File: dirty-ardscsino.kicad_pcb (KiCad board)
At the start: 2 copper layers, 42.7 x 75.2 mm, 16 parts, among them J1 SCSI, J2 171825-4 (Ext. Power), J3 DM3AT-SF-PEJM5, U1 STM32 Bluepill

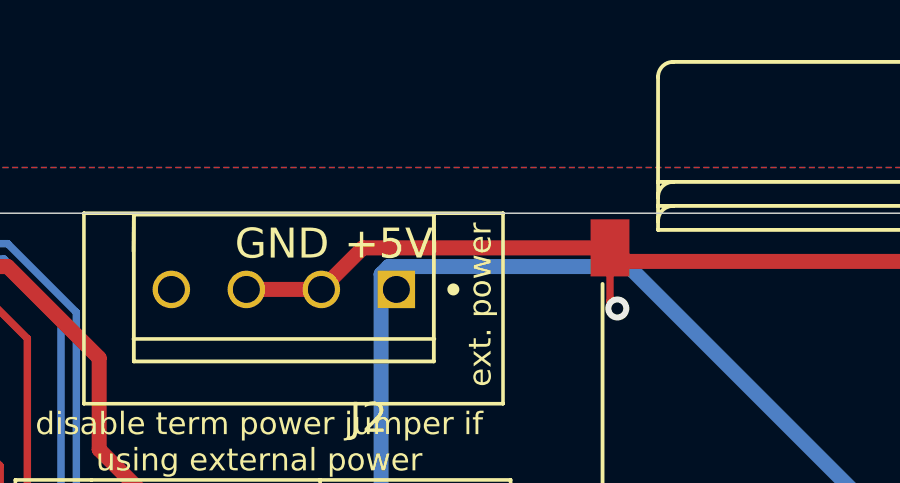
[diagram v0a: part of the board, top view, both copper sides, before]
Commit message: Flip power labels so you can read them
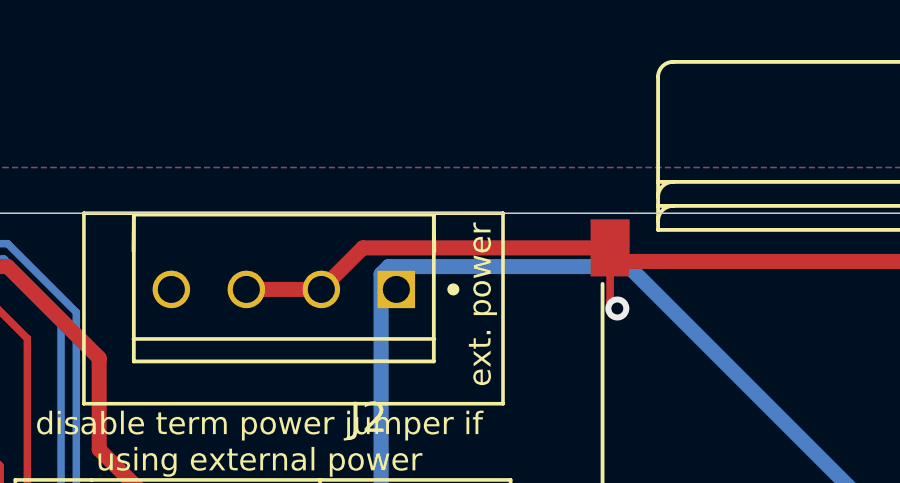
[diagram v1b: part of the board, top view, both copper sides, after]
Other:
- net class Default removed

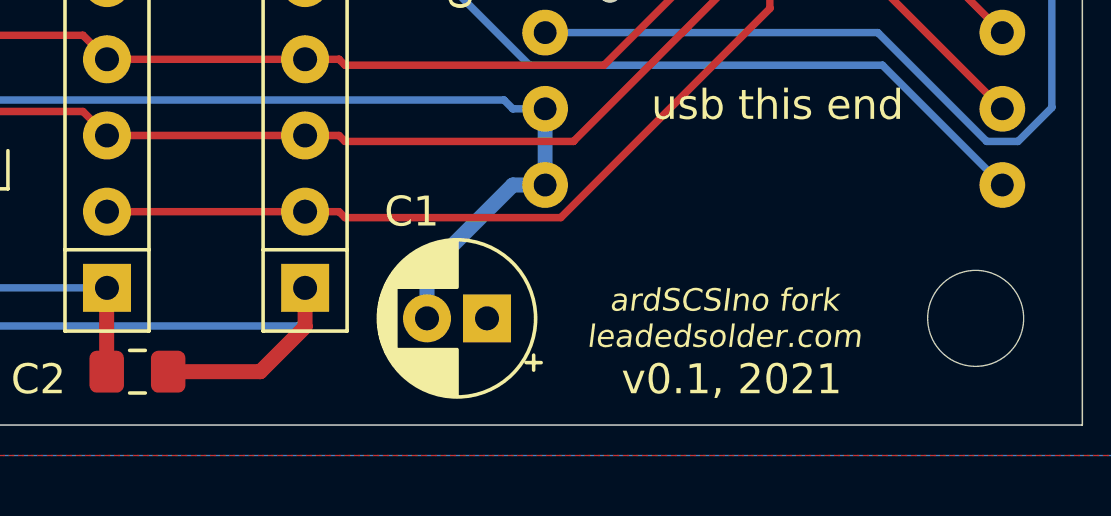
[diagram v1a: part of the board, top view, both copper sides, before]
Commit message: Improve assembly labeling
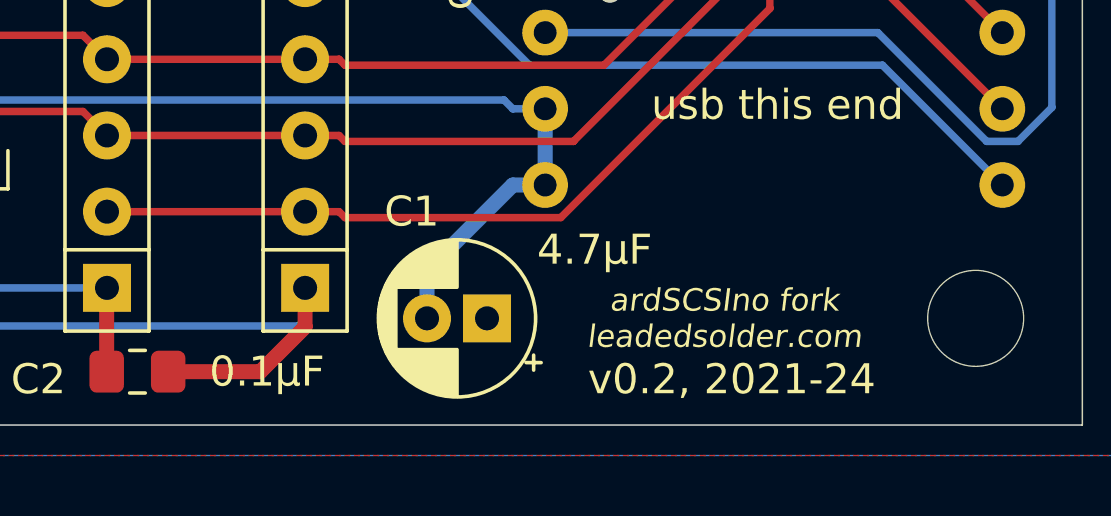
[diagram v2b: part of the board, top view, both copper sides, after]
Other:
- board text added: "v0.2, 2021-24"
- board text removed: "v0.1, 2021"
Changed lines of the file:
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@@
         (effects (font (size 1 1) (thickness 0.15)))
     )
-    (fp_text value "4.7µF" (at -0.762 3.81) (layer "F.Fab")
+    (fp_text value "4.7µF" (at -3.588 2.286) (layer "F.SilkS")
         (effects (font (size 1 1) (thickness 0.15)))
     )
@@
         (effects (font (size 1 1) (thickness 0.15)))
     )
-    (fp_text value "0.1µF" (at 0 1.65) (layer "F.Fab")
+    (fp_text value "0.1µF" (at 4.318 0) (layer "F.SilkS")
         (effects (font (size 1 1) (thickness 0.15)))
     )
@@
     (effects (font (size 0.75 0.75) (thickness 0.15)))
   )
-  (gr_text "v0.1, 2021" (at 165.1 149.86) (layer "F.SilkS")
+  (gr_text "v0.2, 2021-24" (at 165.1 149.86) (layer "F.SilkS")
     (effects (font (size 1 1) (thickness 0.15)))
   )

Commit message: Dirty ArdSCSIno 2 v1 sent to fab
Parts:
- removed JP2, JP3: Jumper_NC_Small, Connector_PinHeader_2.54mm:PinHeader_1x02_P2.54mm_Vertical
- removed REF** (x2): MountingHole_3.2mm_M3, MountingHole:MountingHole_3.2mm_M3
- removed REF**: OSHW-Logo2_14.6x12mm_SilkScreen, Symbol:OSHW-Logo2_14.6x12mm_SilkScreen
- added JP4: Jumper_2_Small_Bridged, Jumper:SolderJumper-2_P1.3mm_Bridged_RoundedPad1.0x1.5mm, F.Cu at (143.3, 118.5)
- added JP5: Jumper_2_Small_Bridged, Jumper:SolderJumper-2_P1.3mm_Bridged_RoundedPad1.0x1.5mm, F.Cu at (143.3, 122.0)
- added U2: microSD-Breakout, microSD_Breakout:microSD_AliExpress, F.Cu at (152.7, 93.8)
- C2: footprint Capacitor_SMD:C_0805_2012Metric_Pad1.15x1.40mm_HandSolder -> Capacitor_SMD:C_0805_2012Metric_Pad1.18x1.45mm_HandSolder
- JP1: value Jumper_NC_Small -> TERM_PWR_EN
- moved C2 100.5 mm to (122.5, 51.8), turned to 180 degrees
- moved J2 64.9 mm to (112.0, 127.0), turned to 90 degrees
- moved RN1 52.2 mm to (120.0, 55.0)
- moved RN2 46.3 mm to (125.0, 55.0)
- moved J1 43.8 mm to (106.7, 113.5)
- moved U1 43.5 mm to (139.0, 87.3)
- moved C1 43.4 mm to (119.2, 126.2), turned to 90 degrees
- moved RN4 41.9 mm to (120.0, 118.5)
- moved JP1 39.4 mm to (134.2, 124.7), turned to 0 degrees
- moved RN3 34.2 mm to (125.0, 118.5)
- moved J3 32.7 mm to (152.7, 120.4), turned to 90 degrees
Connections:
- C2 pad 1: Net-(C2-Pad1) -> GND
- C2 pad 2: Net-(C2-Pad2) -> +5V
- J1 pad 25: Net-(J1-Pad25) -> unconnected-(J1-Pin_25-Pad25)
- J2 pad 4: Net-(J2-Pad4) -> unconnected-(J2-Pad4)
- J3 pad 1: Net-(J3-Pad1) -> unconnected-(J3-DAT2-Pad1)
- J3 pad 8: Net-(J3-Pad8) -> unconnected-(J3-DAT1-Pad8)
- J3 pad SWA: Net-(J3-PadSWA) -> unconnected-(J3-PadSWA)
- J3 pad SWB: Net-(J3-PadSWB) -> unconnected-(J3-PadSWB)
- RN1 pad 1: Net-(C2-Pad2) -> +5V
- RN2 pad 1: Net-(C2-Pad1) -> GND
- RN3 pad 1: Net-(C2-Pad1) -> GND
- RN4 pad 1: Net-(C2-Pad2) -> +5V
- U1 pad NRST: Net-(U1-PadNRST) -> unconnected-(U1-RESET-PadNRST)
- U1 pad PA0: Net-(U1-PadPA0) -> unconnected-(U1-PadPA0)
- U1 pad PA1: Net-(U1-PadPA1) -> unconnected-(U1-PadPA1)
- U1 pad PA11: Net-(U1-PadPA11) -> unconnected-(U1-PadPA11)
- U1 pad PA12: Net-(U1-PadPA12) -> unconnected-(U1-PadPA12)
- U1 pad PA2: Net-(U1-PadPA2) -> unconnected-(U1-PadPA2)
- U1 pad PA3: Net-(U1-PadPA3) -> unconnected-(U1-PadPA3)
- U1 pad PA6: /SD_MISO -> /BP_MISO
- U1 pad PA7: /SD_MOSI -> /BP_MOSI
- U1 pad PB1: Net-(U1-PadPB1) -> unconnected-(U1-PadPB1)
- U1 pad PC13: Net-(U1-PadPC13) -> unconnected-(U1-PadPC13)
- U1 pad PC14: Net-(U1-PadPC14) -> unconnected-(U1-PadPC14)
- U1 pad PC15: Net-(U1-PadPC15) -> unconnected-(U1-PadPC15)
- U1 pad VBAT: Net-(U1-PadVBAT) -> unconnected-(U1-Vbat-PadVBAT)
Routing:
- net Net-(C2-Pad2): track 126.2 -> 0.00 mm
- net Net-(C2-Pad1): track 111.0 -> 0.00 mm
- net GND: track 99.5 -> 12.8 mm, vias 2 -> 5
- net /SD_CS: track 28.4 -> 92.0 mm, vias 1 -> 3
- net /SD_CSK: track 30.5 -> 90.4 mm, vias 1 -> 3
- net +5V: track 51.1 -> 4.15 mm, vias 1 -> 0
- net /SD_VCC: track 76.6 -> 123.5 mm, vias 1 -> 6
- net /BP_MISO: track 0.00 -> 45.1 mm, vias 0 -> 2
- net /SCSI_DAT0: track 66.2 -> 109.6 mm, vias 1 -> 2
- net /SCSI_DAT1: track 66.8 -> 109.0 mm, vias 1 -> 2
- net /BP_MOSI: track 0.00 -> 39.7 mm, vias 0 -> 2
- net /SCSI_DAT3: track 23.0 -> 51.2 mm, vias 0 -> 4
- net /TERM_POWER: track 61.7 -> 88.4 mm
- net /SCSI_DAT2: track 32.0 -> 49.4 mm, vias 1 -> 2
- net /SD_MISO: track 34.1 -> 45.3 mm, vias 1 -> 2
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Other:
- board size 42.7 x 75.2 mm -> 70.9 x 82 mm
- rule pad_to_mask_clearance: 0.051 -> 0
- board text added: "dirty ardscsino 2"
- board text added: "leadedsolder.com 2025 v1"
- board text removed: "#1"
- board text removed: "(both) enable scsi termination"
- board text removed: "220Ω"
- board text removed: "330Ω"
- board text removed: "3v3"
- board text removed: "5v"
- board text removed: "ACK"
- board text removed: "ATN"
- board text removed: "Busy"
- board text removed: "CD"
- board text removed: "DBP"
- board text removed: "Data 0"
- board text removed: "Data 1"
- board text removed: "Data 2"
- board text removed: "Data 3"
- board text removed: "Data 4"
- board text removed: "Data 5"
- board text removed: "Data 6"
- board text removed: "Data 7"
- board text removed: "I/O"
- board text removed: "MSG"
- board text removed: "REQ"
- board text removed: "Reset"
- board text removed: "SEL"
- board text removed: "Term. Power"
- board text removed: "ardSCSIno fork leadedsolder.com"
- board text removed: "disable term power jumper if using external power"
- board text removed: "enable term power"
- board text removed: "ext. power"
- board text removed: "files go here"
- board text removed: "original design: github.com/ztto/ArdSCSino-stm32"
- board text removed: "usb this end"
- board text removed: "v0.2, 2021-24"

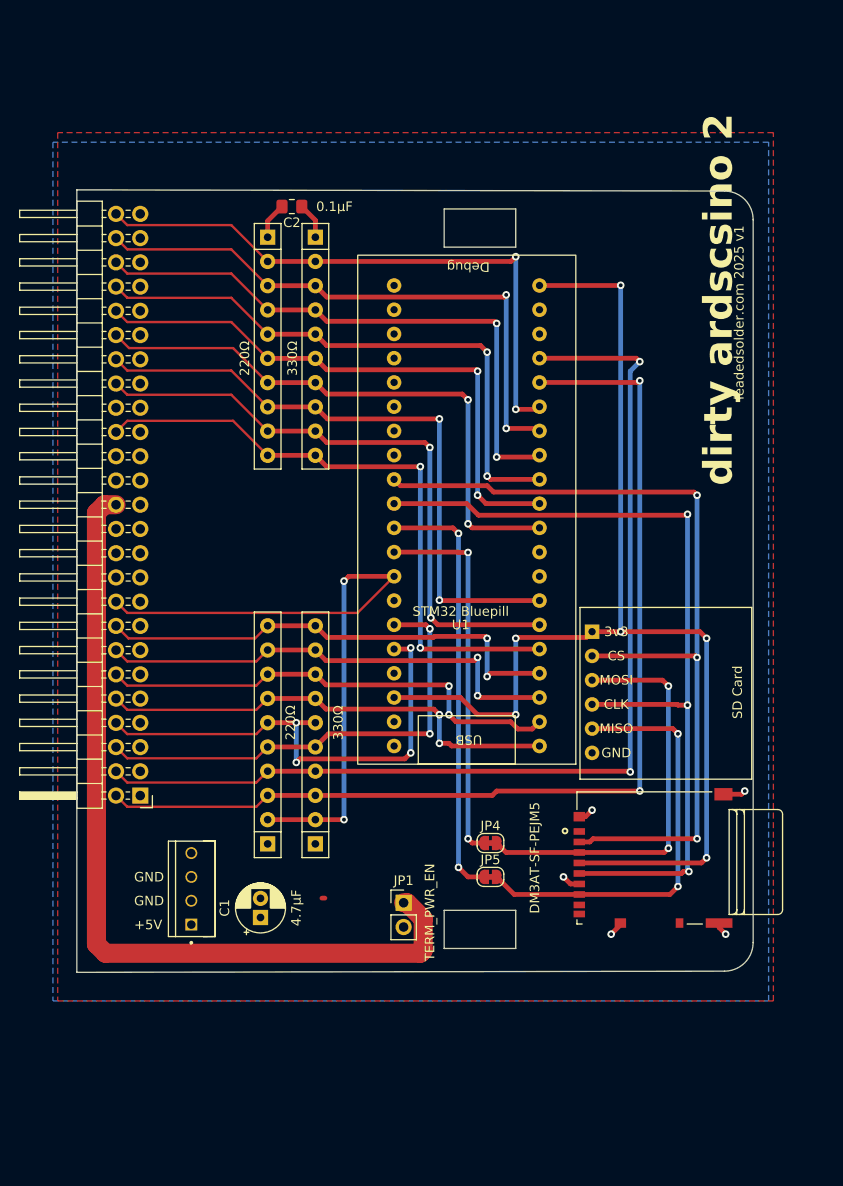
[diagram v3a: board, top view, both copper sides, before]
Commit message: Re-add mounting holes (oops)
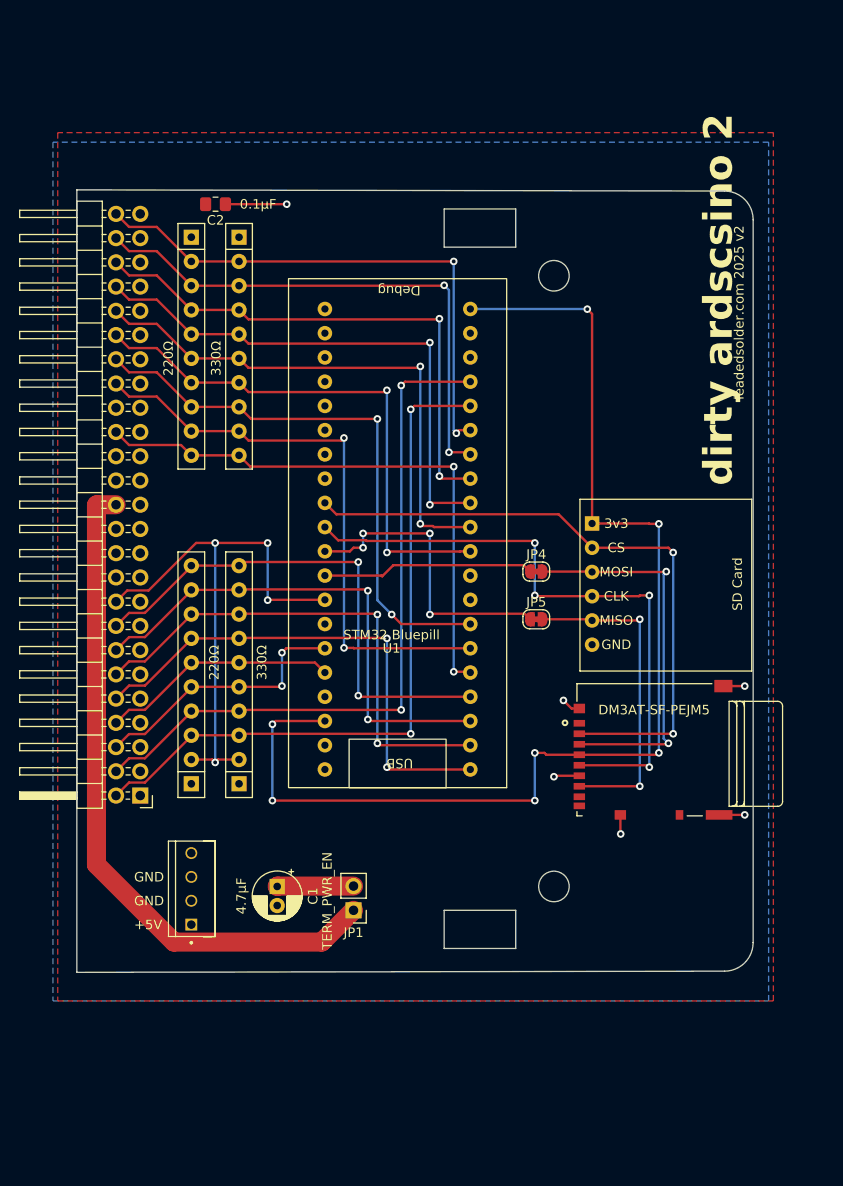
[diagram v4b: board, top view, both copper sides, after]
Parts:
- added REF**: MountingHole_3.2mm_M3_DIN965, MountingHole:MountingHole_3.2mm_M3_DIN965, F.Cu at (150.0, 59.0)
- added REF**: MountingHole_3.2mm_M3_DIN965, MountingHole:MountingHole_3.2mm_M3_DIN965, F.Cu at (150.0, 123.0)
- moved JP4 28.9 mm to (148.2, 90.0)
- moved JP5 27.4 mm to (148.2, 95.0)
- moved J3 11.3 mm to (152.7, 109.1)
- moved U2 11.3 mm to (152.7, 82.4)
- moved RN3 10.2 mm to (117.0, 112.2)
- moved RN4 10.2 mm to (112.0, 112.2)
- moved C2 8.00 mm to (114.5, 51.5)
- moved RN1 8.00 mm to (112.0, 55.0)
- moved RN2 8.00 mm to (117.0, 55.0)
- moved U1 7.66 mm to (131.7, 89.8)
- moved JP1 5.31 mm to (129.0, 125.5), turned to 180 degrees
- moved C1 3.69 mm to (121.0, 123.0), turned to -90 degrees
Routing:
- net /SCSI_DAT0: track 109.6 -> 74.0 mm
- net /SCSI_DAT1: track 109.0 -> 74.0 mm
- net /SCSI_DAT3: track 51.2 -> 25.0 mm, vias 4 -> 0
- net /SD_CSK: track 90.4 -> 65.7 mm, vias 3 -> 4
- net /SD_CS: track 92.0 -> 67.5 mm, vias 3 -> 2
- net /SCSI_DAT2: track 49.4 -> 28.3 mm
- net /BP_MOSI: track 39.7 -> 22.3 mm, vias 2 -> 0
- net /TERM_POWER: track 88.4 -> 71.4 mm
- net /BP_MISO: track 45.1 -> 31.9 mm, vias 2 -> 4
- net /SD_MISO: track 45.3 -> 34.1 mm
- net /SCSI_DBP: track 69.7 -> 58.7 mm, vias 2 -> 4
- net /SCSI_ACK: track 66.0 -> 59.8 mm
- net /SCSI_ATN: track 65.9 -> 60.2 mm
- net /SCSI_IO: track 62.8 -> 57.2 mm
- net GND: track 12.8 -> 18.1 mm, vias 5 -> 6
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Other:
- board text added: "leadedsolder.com 2025 v2"
- board text removed: "leadedsolder.com 2025 v1"

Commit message: Label the term. power pin
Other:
- board text added: "TP"
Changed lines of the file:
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@@
+		)
+	)
+	(gr_text "TP"
+		(at 101 82.39325 180)
+		(layer "B.SilkS")
+		(effects
+			(font
+				(size 1 1)
+				(thickness 0.15)
+			)
+			(justify left bottom mirror)
 		)
 	)
